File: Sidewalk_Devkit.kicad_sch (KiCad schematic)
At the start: 5 parts, among them SW1 SW_Push

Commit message: Updates for rev 1
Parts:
- added TP1: TestPoint, TestPoint:TestPoint_Keystone_5015_Micro_Mini, symbol Connector:TestPoint
- added TP2: TestPoint, TestPoint:TestPoint_Pad_D1.0mm, symbol Connector:TestPoint
- SW1: LCSC (none) -> C127488
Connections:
- net BUTTON0: now also TP2.1
- net GND: now also TP1.1
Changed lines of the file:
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@@
 	(generator_version "10.0")
 	(paper "A4")
+	(junction
+		(at 83.82 132.08)
+		(diameter 0)
+		(color 0 0 0 0)
+	)
+	(junction
+		(at 83.82 121.92)
+		(diameter 0)
+		(color 0 0 0 0)
+	)
 	(bus
 		(pts
@@
 			)
 		)
+		(property "LCSC" "C127488"
+			(at 83.82 127 90)
+			(hide yes)
+			(show_name no)
+			(do_not_autoplace no)
+			(effects
+				(font
+					(size 1.27 1.27)
+				)
+			)
+		)
 		(pin "2"
 		)
@@
 				(path "/46ec7b9e-7ce4-471b-b2a3-117ade628de1"
 					(reference "SW1")
+					(unit 1)
+				)
+			)
+		)
+	)
+	(symbol
+		(lib_id "Connector:TestPoint")
+		(at 83.82 121.92 90)
+		(unit 1)
+		(body_style 1)
+		(exclude_from_sim no)
+		(in_bom no)
+		(on_board yes)
+		(in_pos_files no)
+		(dnp yes)
+		(property "Reference" "TP2"
+			(at 78.74 121.92 90)
+			(show_name no)
+			(do_not_autoplace no)
+			(effects
+				(font
+					(size 1.27 1.27)
+				)
+				(justify left)
+			)
+		)
+		(property "Value" "TestPoint"
+			(at 78.74 120.6501 90)
+			(hide yes)
+			(show_name no)
+			(do_not_autoplace no)
+			(effects
+				(font
+					(size 1.27 1.27)
+				)
+				(justify left)
+			)
+		)
+		(property "Footprint" "TestPoint:TestPoint_Pad_D1.0mm"
+			(at 83.82 116.84 0)
+			(hide yes)
+			(show_name no)
+			(do_not_autoplace no)
+			(effects
+				(font
+					(size 1.27 1.27)
+				)
+			)
+		)
+		(property "Datasheet" ""
+			(at 83.82 116.84 0)
+			(hide yes)
+			(show_name no)
+			(do_not_autoplace no)
+			(effects
+				(font
+					(size 1.27 1.27)
+				)
+			)
+		)
+		(property "Description" "test point"
+			(at 83.82 121.92 0)
+			(hide yes)
+			(show_name no)
+			(do_not_autoplace no)
+			(effects
+				(font
+					(size 1.27 1.27)
+				)
+			)
+		)
+		(pin "1"
+		)
+		(instances
+			(project "Sidewalk_Devkit"
+				(path "/46ec7b9e-7ce4-471b-b2a3-117ade628de1"
+					(reference "TP2")
 					(unit 1)
 				)
@@
 					(unit 1)
 				)
+			)
+		)
+	)
+	(symbol
+		(lib_id "Connector:TestPoint")
+		(at 83.82 132.08 270)
+		(unit 1)
+		(body_style 1)
+		(exclude_from_sim no)
+		(in_bom no)
+		(on_board yes)
+		(in_pos_files no)
+		(dnp yes)
+		(property "Reference" "TP1"
+			(at 88.9 132.08 90)
+			(show_name no)
+			(do_not_autoplace no)
+			(effects
+				(font
+					(size 1.27 1.27)
+				)
+				(justify left)
+			)
+		)
+		(property "Value" "TestPoint"
+			(at 88.9 133.3499 90)
+			(hide yes)
+			(show_name no)
+			(do_not_autoplace no)
+			(effects
+				(font
+					(size 1.27 1.27)
+				)
+				(justify left)
+			)
+		)
+		(property "Footprint" "TestPoint:TestPoint_Keystone_5015_Micro_Mini"
+			(at 83.82 137.16 0)
+			(hide yes)
+			(show_name no)
+			(do_not_autoplace no)
+			(effects
+				(font
+					(size 1.27 1.27)
+				)
+			)
+		)
+		(property "Datasheet" ""
+			(at 83.82 137.16 0)
+			(hide yes)
+			(show_name no)
+			(do_not_autoplace no)
+			(effects
+				(font
+					(size 1.27 1.27)
+				)
+			)
+		)
+		(property "Description" "test point"
+			(at 83.82 132.08 0)
+			(hide yes)
+			(show_name no)
+			(do_not_autoplace no)
+			(effects
+				(font
+					(size 1.27 1.27)
+				)
+			)
+		)
+		(pin "1"
+		)
+		(instances
+			(project "Sidewalk_Devkit"
+				(path "/46ec7b9e-7ce4-471b-b2a3-117ade628de1"
+					(reference "TP1")
+					(unit 1)
+				)

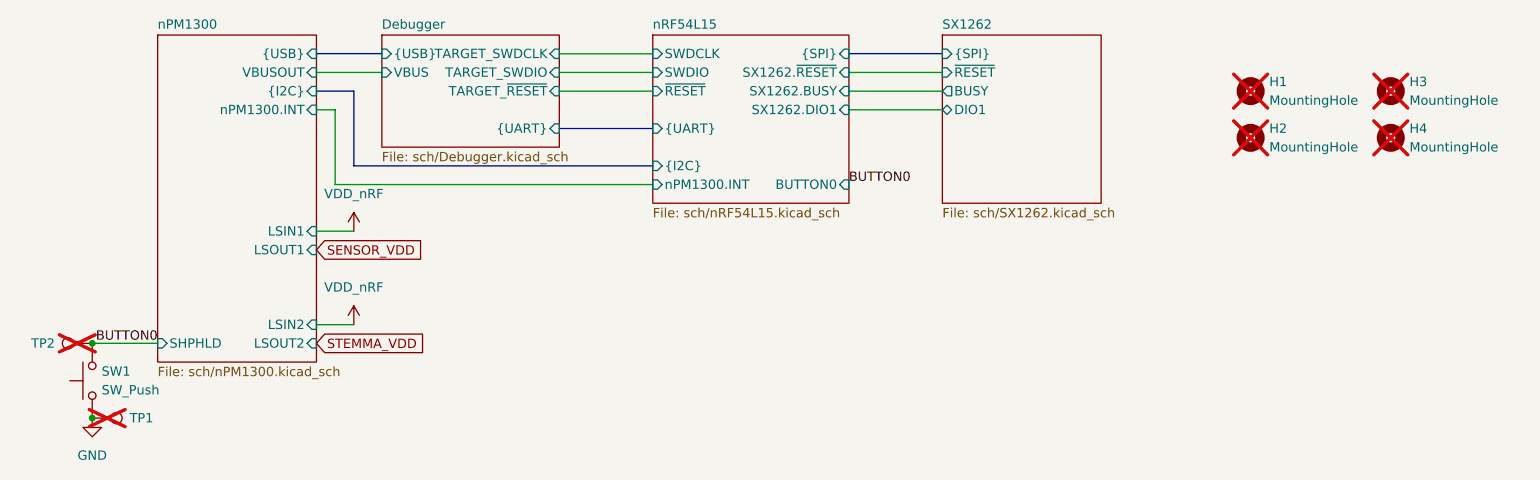
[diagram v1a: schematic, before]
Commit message: Added external current measurement for L15 and SX1262
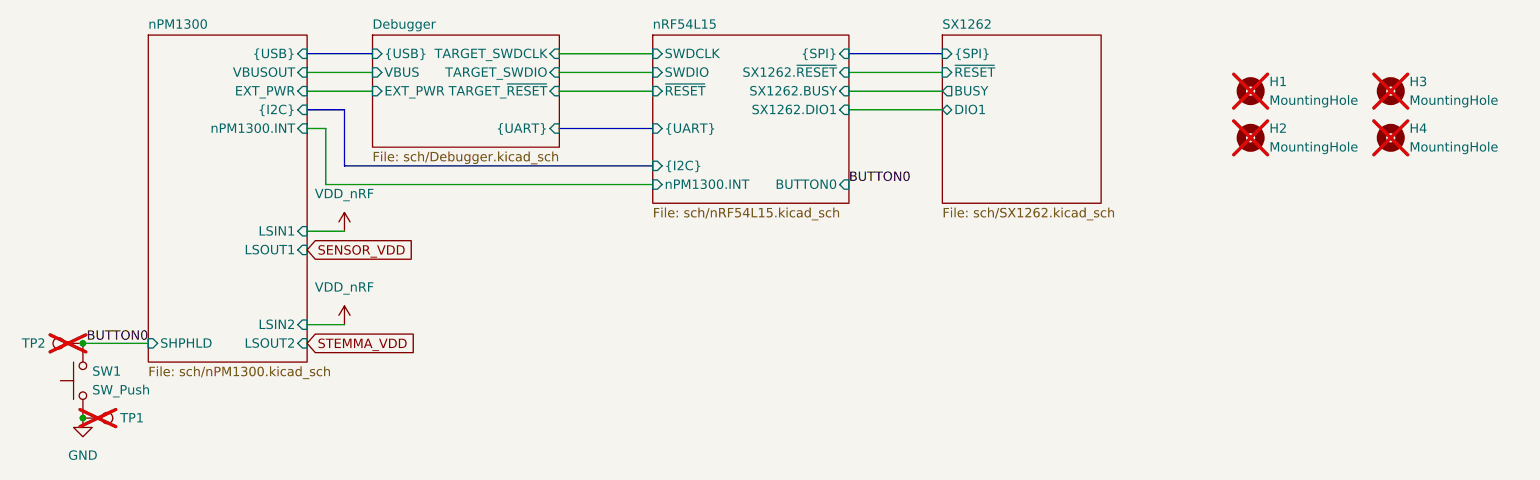
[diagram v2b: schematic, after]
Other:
- sheet Debugger ports: added EXT_PWR; removed none
- sheet nPM1300 ports: added EXT_PWR; removed none
- moved on the sheet: SW1, TP1, TP2
